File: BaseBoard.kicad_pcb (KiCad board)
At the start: 2 copper layers, 225 x 225 mm, 162 parts, among them J1 OSTTC022162, Q1 MMBT2222A-7-F, Q10 IRLML6401TRPBF, Q11 MMBT2222A-7-F, Q12 IRLML6401TRPBF, Q13 MMBT2222A-7-F, Q14 IRLML6401TRPBF, Q15 MMBT2222A-7-F, Q16 IRLML6401TRPBF, Q2 IRLML6401TRPBF, Q3 MMBT2222A-7-F, Q4 IRLML6401TRPBF, Q5 MMBT2222A-7-F, Q6 IRLML6401TRPBF, Q7 MMBT2222A-7-F, Q8 IRLML6401TRPBF, Q9 MMBT2222A-7-F, U1 TLC5971PWPR, U10 TLC5971PWPR, U11 TLC5971PWPR, U12 TLC5971PWPR, U13 TLC5971PWPR, U14 TLC5971PWPR, U15 TLC5971PWPR, U16 TLC5971PWPR, U2 TLC5971PWPR, U3 TLC5971PWPR, U4 TLC5971PWPR, U5 TLC5971PWPR, U6 TLC5971PWPR, U7 TLC5971PWPR, U8 TLC5971PWPR, U9 TLC5971PWPR

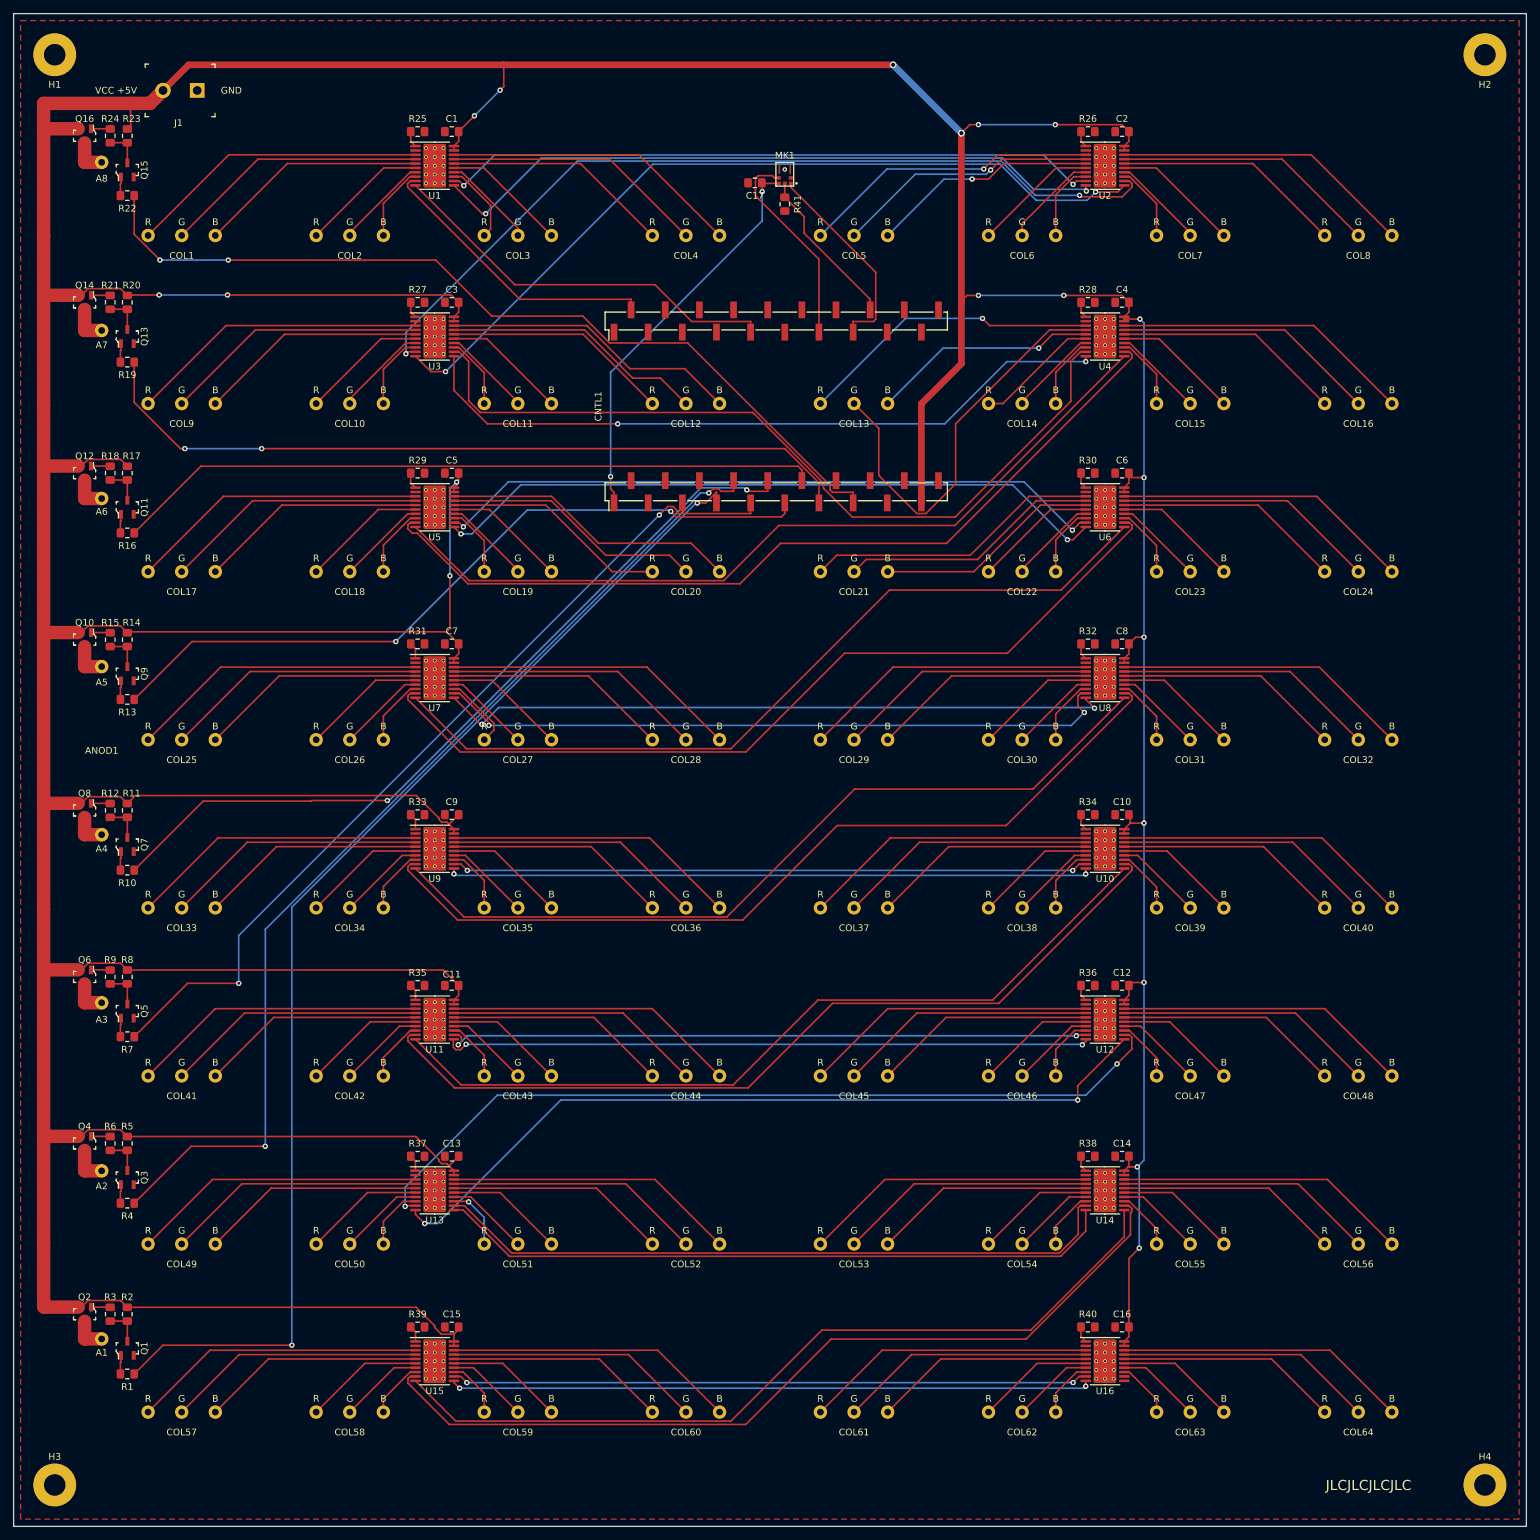
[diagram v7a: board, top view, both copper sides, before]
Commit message: Add zone to back copper layer
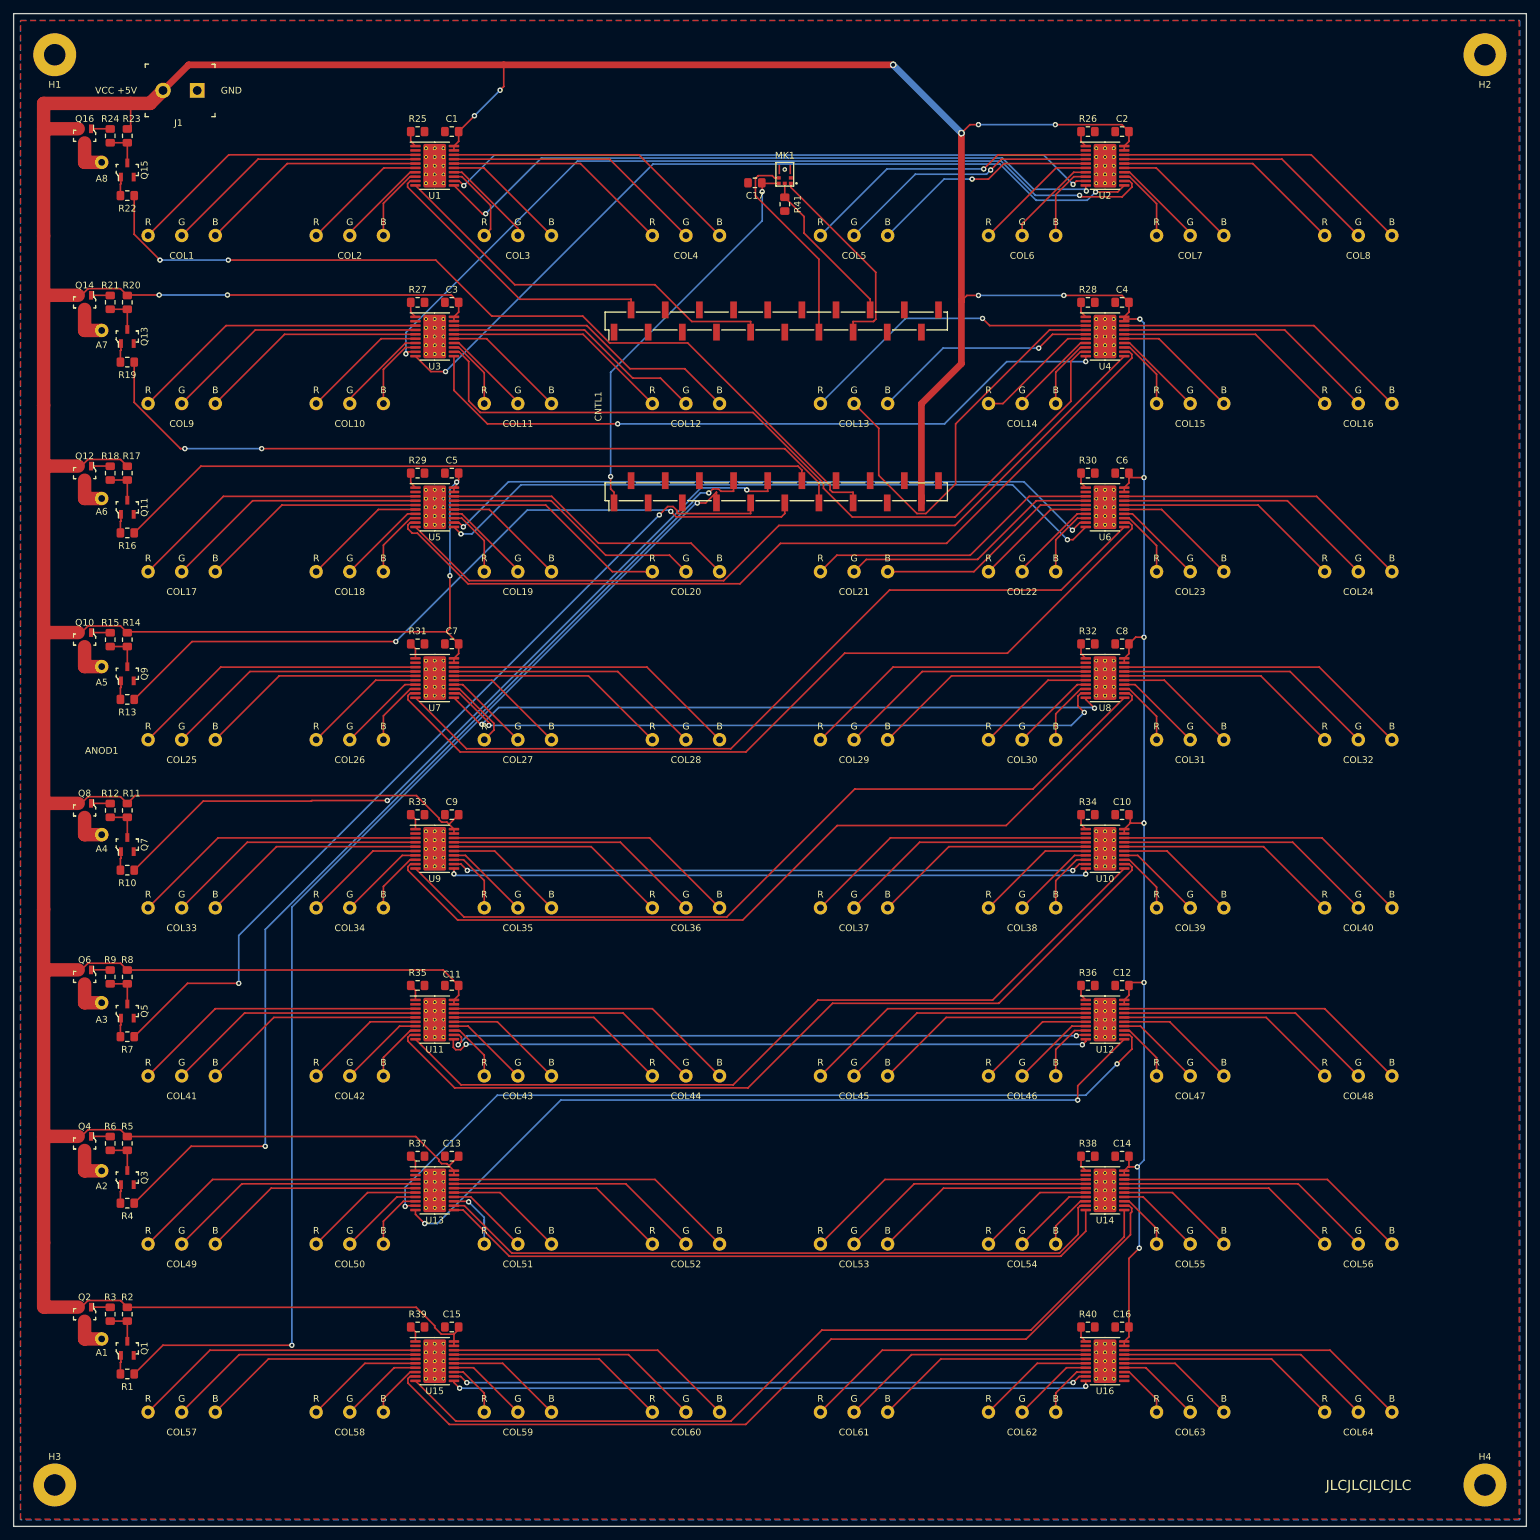
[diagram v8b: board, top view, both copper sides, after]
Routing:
- added copper zone on B.Cu, net GND
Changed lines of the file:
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@@
-(kicad_pcb (version 20171130) (host pcbnew "(5.1.5-0-10_14)")
+(kicad_pcb (version 20171130) (host pcbnew "(5.1.5)-3")
   (general
     (thickness 1.6)
@@
       )
     )
+  )
+  (zone (net 195) (net_name GND) (layer B.Cu) (hatch edge 0.508)
+    (connect_pads yes (clearance 0.254))
+    (min_thickness 0.254)
+    (fill yes (arc_segments 32) (thermal_gap 0.508) (thermal_bridge_width 0.508))
+    (polygon
+      (pts
+        (xy 243.948 243.948) (xy 20.936 243.948) (xy 20.936 20.936) (xy 243.948 20.936)
+      )
+    )
